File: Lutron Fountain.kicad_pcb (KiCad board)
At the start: 2 copper layers, 98 parts, among them Q1 BC547, Q10 BC547, Q11 BC547, Q12 BC547, Q13 BC547, Q14 BC547, Q15 BC547, Q16 BC547, Q17 BC547, Q18 BC547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

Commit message: pcb finished
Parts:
- added J1: Barrel_Jack_MountingPin, Connector_BarrelJack:BarrelJack_CUI_PJ-102AH_Horizontal, F.Cu at (128.6, 59.8)
- moved R20 187.0 mm to (222.6, 147.6), turned to 90 degrees
- moved D7 186.9 mm to (214.2, 87.0), turned to 180 degrees
- moved D16 186.8 mm to (214.2, 100.8), turned to 180 degrees
- moved R10 179.1 mm to (222.2, 40.0), turned to -90 degrees
- moved R18 178.0 mm to (207.7, 147.9), turned to 90 degrees
- moved R9 173.5 mm to (217.5, 74.9), turned to -90 degrees
- moved D5 173.1 mm to (198.9, 86.6), turned to 180 degrees
- moved D14 172.8 mm to (198.3, 101.3), turned to 180 degrees
- moved R19 170.7 mm to (217.6, 113.2), turned to 90 degrees
- moved D18 170.5 mm to (222.5, 130.2), turned to -90 degrees
- moved D10 170.1 mm to (222.8, 58.6), turned to 90 degrees
- moved R16 169.8 mm to (192.6, 147.6), turned to 90 degrees
- moved D8 165.7 mm to (207.8, 58.9), turned to 90 degrees
- moved R8 163.8 mm to (207.7, 40.1), turned to -90 degrees
- moved R14 163.4 mm to (177.9, 147.8), turned to 90 degrees
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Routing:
- net +5V: track 0.00 -> 544.5 mm
- net Net-(D1-A): track 0.00 -> 40.9 mm
- net Net-(D19-A): track 0.00 -> 37.4 mm
- net Net-(Q9-B): track 0.00 -> 12.8 mm
- net Net-(D14-K): track 0.00 -> 12.7 mm
- net Net-(D20-K): track 0.00 -> 12.3 mm
- net Net-(Q6-B): track 0.00 -> 12.2 mm
- net Net-(Q7-B): track 0.00 -> 11.9 mm
- net Net-(D19-K): track 0.00 -> 11.8 mm
- net Net-(D12-K): track 0.00 -> 11.7 mm
- net Net-(Q8-B): track 0.00 -> 11.7 mm
- net Net-(Q15-B): track 0.00 -> 11.5 mm
- net Net-(D5-K): track 0.00 -> 11.5 mm
- net Net-(D27-K): track 0.00 -> 11.4 mm
- net Net-(Q12-B): track 0.00 -> 11.4 mm
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- added copper zone on F.Cu, net GND
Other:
- board text added: "Lutron Competition 2026 Anna Tretiakova Annalisa Emanuele"

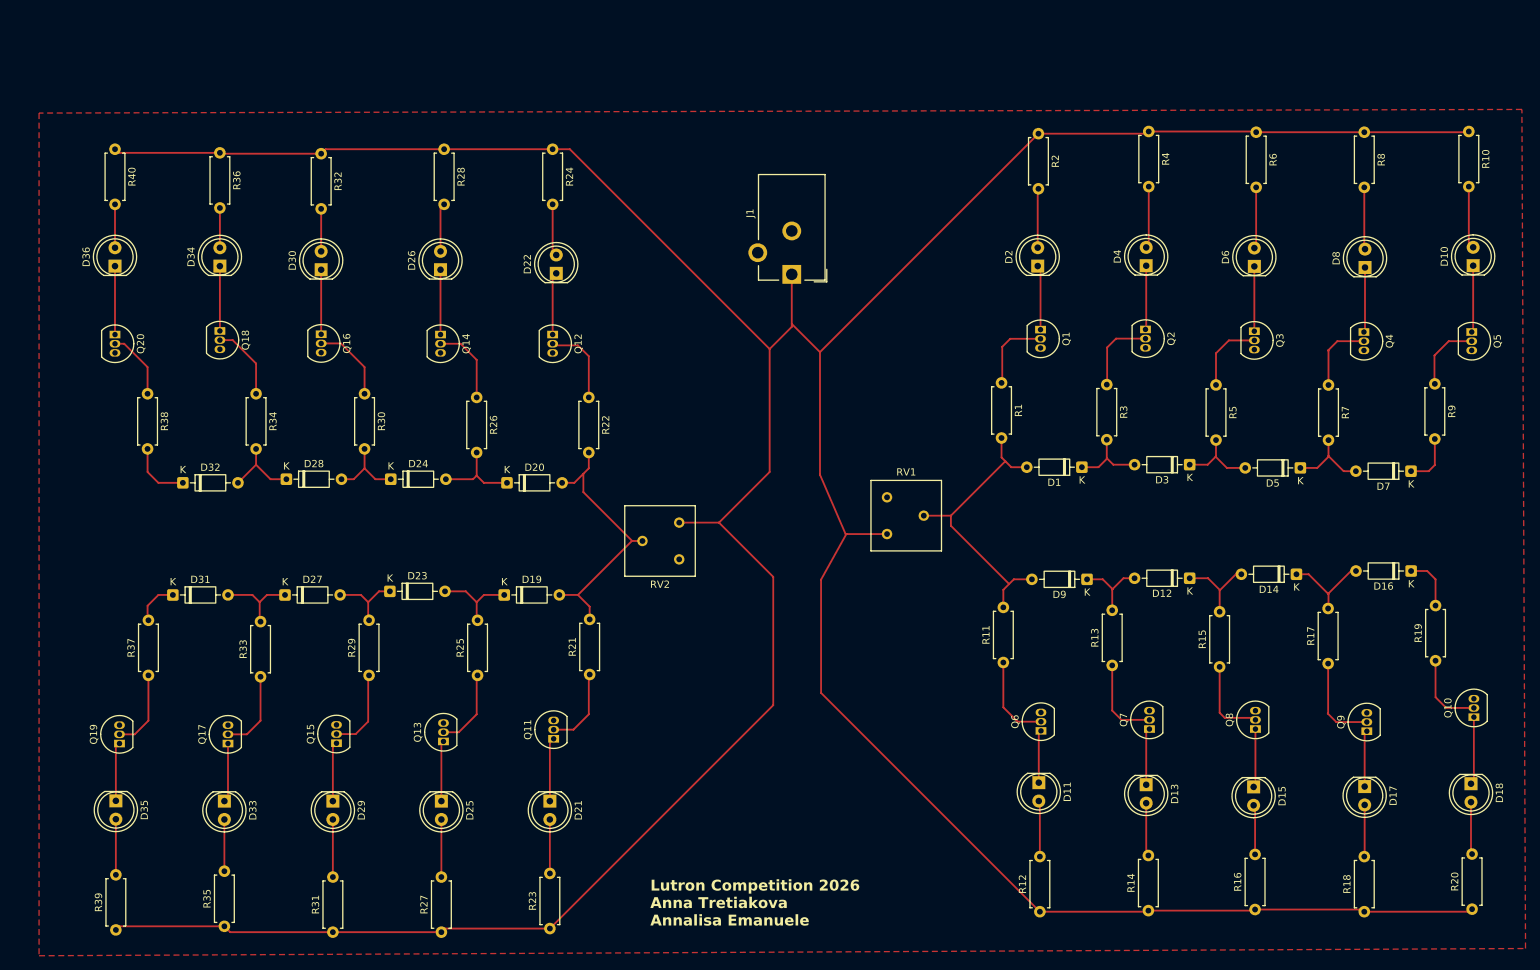
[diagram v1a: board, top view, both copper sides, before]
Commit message: made shared gnd
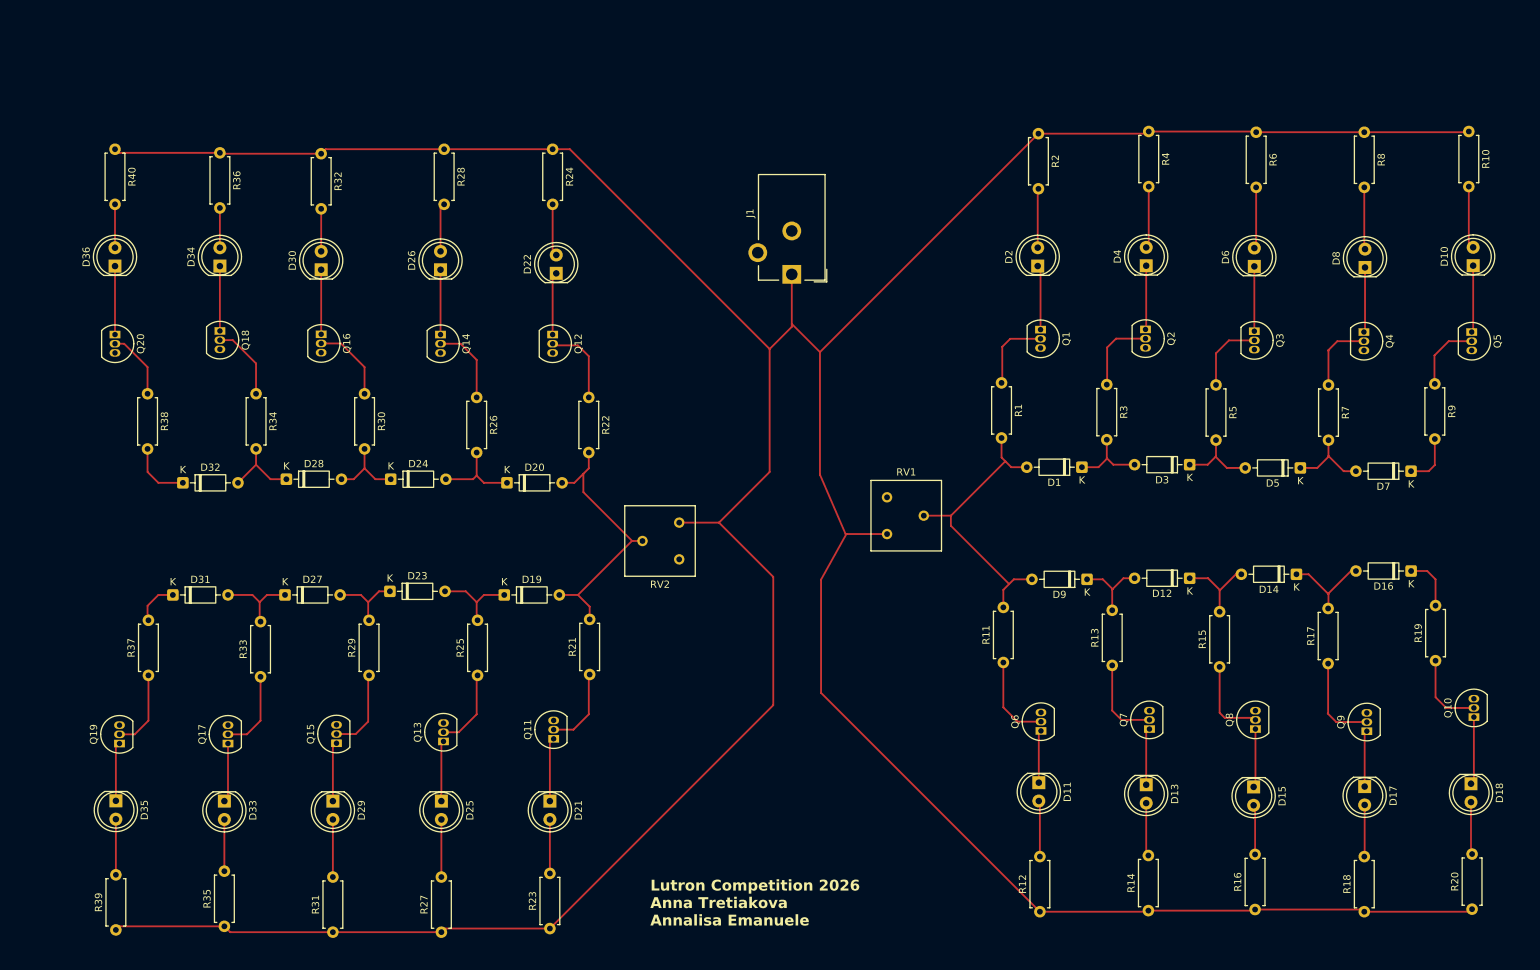
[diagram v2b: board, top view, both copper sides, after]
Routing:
- added copper zone on In1.Cu, net GND
- removed copper zone on F.Cu, net GND
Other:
- copper layers 2 -> 4
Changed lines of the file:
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@@
 	(layers
 		(0 "F.Cu" signal)
+		(4 "In1.Cu" signal)
+		(6 "In2.Cu" signal)
 		(2 "B.Cu" signal)
 		(9 "F.Adhes" user "F.Adhesive")
@@
 	)
 	(setup
+		(stackup
+			(layer "F.SilkS"
+				(type "Top Silk Screen")
+			)
+			(layer "F.Paste"
+				(type "Top Solder Paste")
+			)
+			(layer "F.Mask"
+				(type "Top Solder Mask")
+				(thickness 0.01)
+			)
+			(layer "F.Cu"
+				(type "copper")
+				(thickness 0.035)
+			)
+			(layer "dielectric 1"
+				(type "prepreg")
+				(thickness 0.1)
+				(material "FR4")
+				(epsilon_r 4.5)
+				(loss_tangent 0.02)
+			)
+			(layer "In1.Cu"
+				(type "copper")
+				(thickness 0.035)
+			)
+			(layer "dielectric 2"
+				(type "core")
+				(thickness 1.24)
+				(material "FR4")
+				(epsilon_r 4.5)
+				(loss_tangent 0.02)
+			)
+			(layer "In2.Cu"
+				(type "copper")
+				(thickness 0.035)
+			)
+			(layer "dielectric 3"
+				(type "prepreg")
+				(thickness 0.1)
+				(material "FR4")
+				(epsilon_r 4.5)
+				(loss_tangent 0.02)
+			)
+			(layer "B.Cu"
+				(type "copper")
+				(thickness 0.035)
+			)
+			(layer "B.Mask"
+				(type "Bottom Solder Mask")
+				(thickness 0.01)
+			)
+			(layer "B.Paste"
+				(type "Bottom Solder Paste")
+			)
+			(layer "B.SilkS"
+				(type "Bottom Silk Screen")
+			)
+			(copper_finish "None")
+			(dielectric_constraints no)
+		)
 		(pad_to_mask_clearance 0)
 		(allow_soldermask_bridges_in_footprints no)
@@
 		(net 59)
 		(net_name "GND")
-		(layer "F.Cu")
+		(layer "In1.Cu")
 		(hatch edge 0.5)
 		(connect_pads
@@
 		(min_thickness 0.25)
 		(filled_areas_thickness no)
-		(fill
+		(fill yes
 			(thermal_gap 0.5)
 			(thermal_bridge_width 0.5)
@@
 		(polygon
 			(pts
-				(xy 24.5 37.5) (xy 24.5 154) (xy 230 153) (xy 229.5 37)
+				(xy 30 35) (xy 230 35) (xy 230 155) (xy 30 155)
 			)
 		)

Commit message: added gnd and power
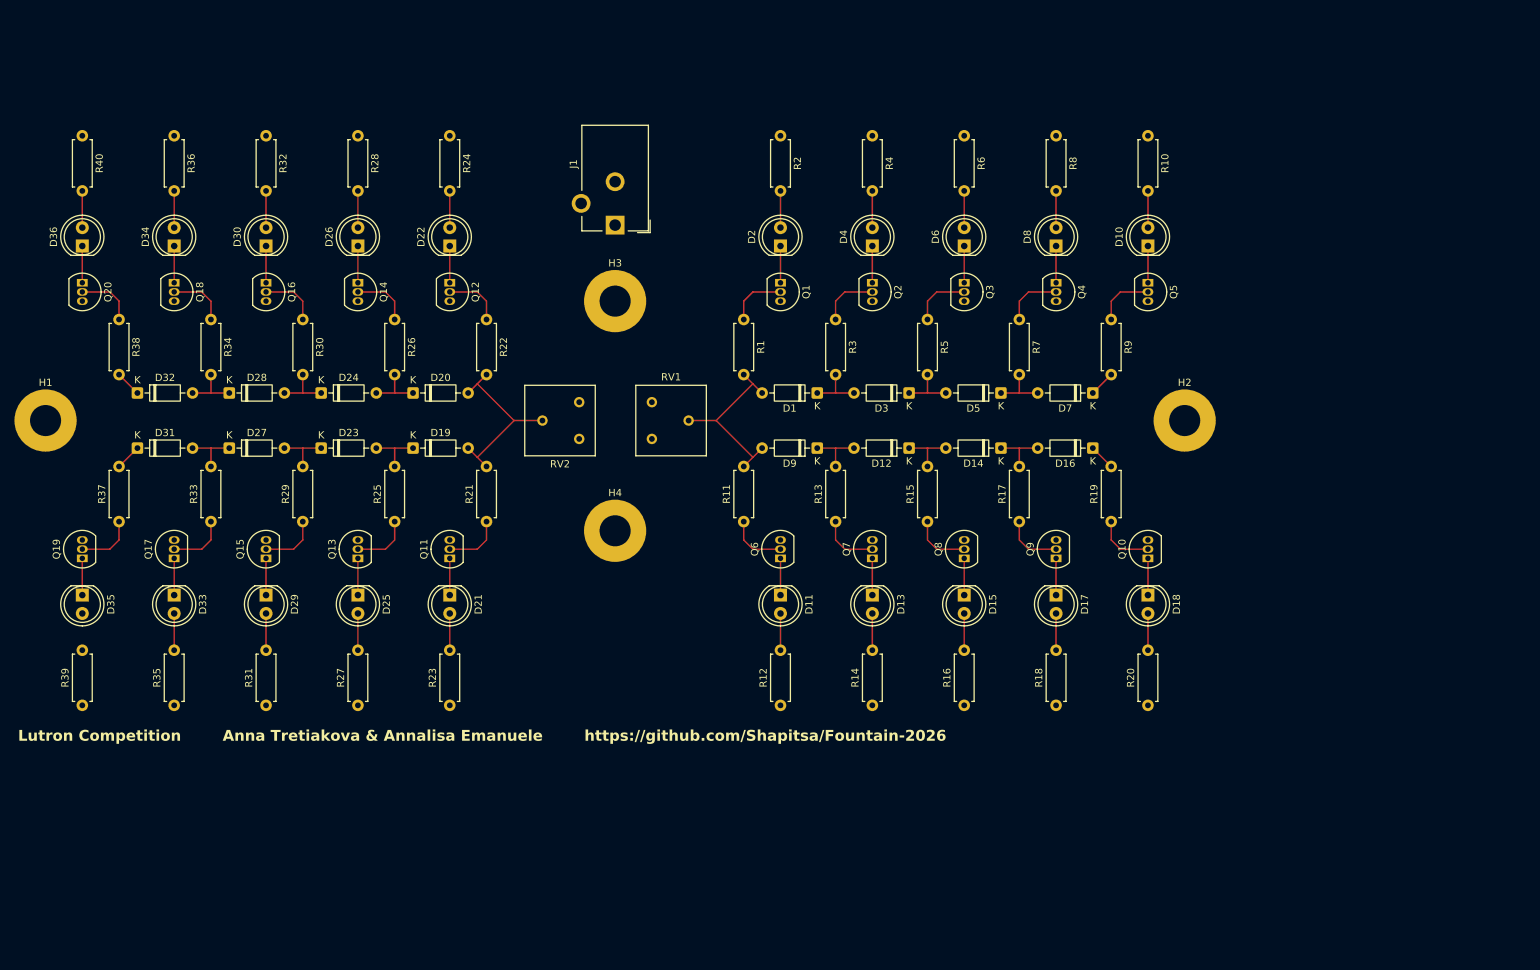
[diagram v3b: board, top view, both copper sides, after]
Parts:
- added H1: MountingHole, MountingHole:MountingHole_4.3mm_M4_Pad, F.Cu at (25.4, 80.0)
- added H2: MountingHole, MountingHole:MountingHole_4.3mm_M4_Pad, F.Cu at (182.9, 80.0)
- added H3: MountingHole, MountingHole:MountingHole_4.3mm_M4_Pad, F.Cu at (104.1, 63.5)
- added H4: MountingHole, MountingHole:MountingHole_4.3mm_M4_Pad, F.Cu at (104.1, 95.2)
- moved R20 52.9 mm to (177.8, 119.4)
- moved D18 51.7 mm to (177.8, 104.1)
- moved R18 51.3 mm to (165.1, 119.4)
- moved D17 50.2 mm to (165.1, 104.1)
- moved Q10 50.1 mm to (177.8, 99.1)
- moved Q9 49.2 mm to (165.1, 99.1)
- moved R16 49.1 mm to (152.4, 119.4)
- moved R19 48.8 mm to (172.7, 94.0)
- moved D15 48.0 mm to (152.4, 104.1)
- moved R14 47.6 mm to (139.7, 119.4)
- moved D16 47.2 mm to (170.2, 83.8)
- moved R17 47.0 mm to (160.0, 94.0)
- moved Q8 46.7 mm to (152.4, 99.1)
- moved D13 46.1 mm to (139.7, 104.1)
- moved R12 45.8 mm to (127.0, 119.4)
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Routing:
- net +5V: track 544.5 -> 0.00 mm
- net Net-(D1-A): track 40.9 -> 25.4 mm
- net Net-(D19-A): track 37.4 -> 25.5 mm
- net Net-(D35-A): track 7.69 -> 0.00 mm
- net Net-(D14-K): track 12.7 -> 7.62 mm
- net Net-(D32-K): track 8.69 -> 3.59 mm
- net Net-(Q9-B): track 12.8 -> 8.15 mm
- net Net-(D20-K): track 12.3 -> 7.62 mm
- net Net-(D36-K): track 9.46 -> 5.08 mm
- net Net-(D18-K): track 9.38 -> 5.08 mm
- net Net-(D10-K): track 9.25 -> 5.08 mm
- net Net-(D19-K): track 11.8 -> 7.62 mm
- net Net-(D12-K): track 11.7 -> 7.62 mm
- net Net-(Q6-B): track 12.2 -> 8.15 mm
- net Net-(D8-K): track 8.98 -> 5.08 mm
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- added copper zone on In2.Cu, net +5V
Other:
- board text added: "Lutron Competition Anna Tretiakova & Annalisa Emanuele https://github.com/Shapitsa/Fountain-2026"
- board text removed: "Lutron Competition 2026 Anna Tretiakova Annalisa Emanuele"
